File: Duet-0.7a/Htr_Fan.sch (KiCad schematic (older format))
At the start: 30 parts, among them J27 TP

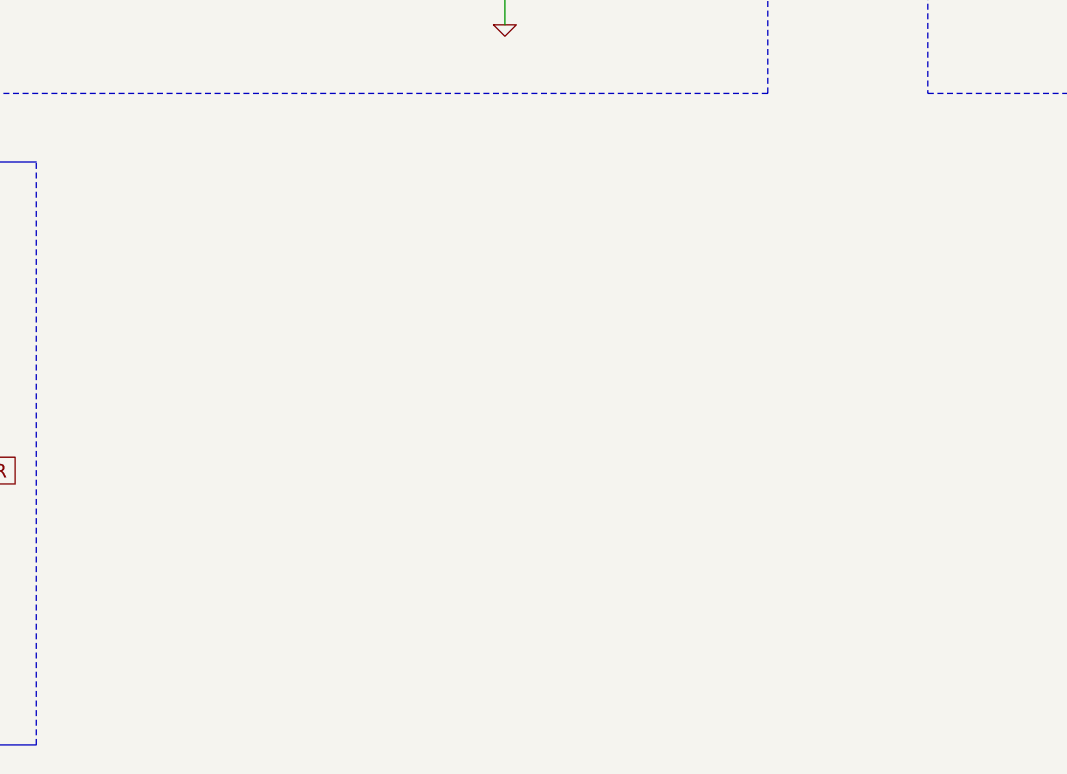
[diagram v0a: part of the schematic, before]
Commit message: Tell-tale LEDs added to Duet 0.7a.
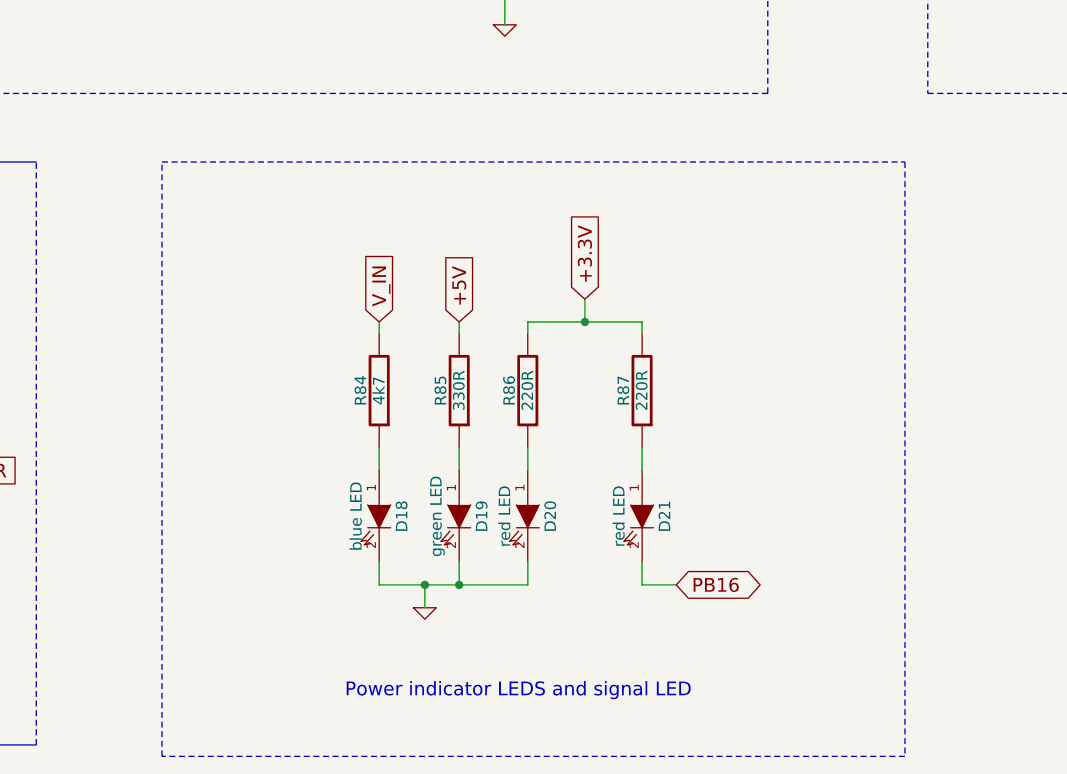
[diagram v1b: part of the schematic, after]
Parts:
- added D18: blue LED, symbol LED
- added D19: green LED, symbol LED
- added D20, D21: red LED, symbol LED
- added R84: 4k7, symbol R
- added R85: 330R, symbol R
- added R86, R87: 220R, symbol R
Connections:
- net labels added: PB16
- wire segments 87 -> 104
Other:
- note added: "Power indicator LEDS and signal LED"
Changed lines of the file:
@@
 LIBS:FE
 LIBS:Duet0.7-cache
-EELAYER 27 0
+EELAYER 24 0
 EELAYER END
 $Descr A3 16535 11693
@@
 FAN0-
 $Comp
-L GND #PWR56
+L GND #PWR054
 U 1 1 5090541F
 P 11600 4450
-F 0 "#PWR56" H 11600 4450 30  0001 C CNN
+F 0 "#PWR054" H 11600 4450 30  0001 C CNN
 F 1 "GND" H 11600 4380 30  0001 C CNN
 F 2 "" H 11600 4450 60  0001 C CNN
@@
 $EndComp
 $Comp
-L GND #PWR55
+L GND #PWR055
 U 1 1 50905416
 P 7400 4450
-F 0 "#PWR55" H 7400 4450 30  0001 C CNN
+F 0 "#PWR055" H 7400 4450 30  0001 C CNN
 F 1 "GND" H 7400 4380 30  0001 C CNN
 F 2 "" H 7400 4450 60  0001 C CNN
@@
 BED-
 $Comp
-L GND #PWR54
+L GND #PWR056
 U 1 1 5064BB75
 P 3300 4450
-F 0 "#PWR54" H 3300 4450 30  0001 C CNN
+F 0 "#PWR056" H 3300 4450 30  0001 C CNN
 F 1 "GND" H 3300 4380 30  0001 C CNN
 F 2 "" H 3300 4450 60  0001 C CNN
@@
 Text GLabel 2250 1800 1    60   Input ~ 0
 +5V
+Wire Wire Line
+	6850 6300 6850 6400
+Wire Wire Line
+	6850 5800 6850 5750
+Wire Wire Line
+	6850 6800 6850 6900
+$Comp
+L LED D18
+U 1 1 5491B59F
+P 6850 6600
+F 0 "D18" H 6850 6700 50  0000 C CNN
+F 1 "blue LED" H 6850 6500 50  0000 C CNN
+F 2 "" H 6850 6600 60  0001 C CNN
+F 3 "" H 6850 6600 60  0001 C CNN
+	1    6850 6600
+	0    1    1    0
+$EndComp
+$Comp
+L R R84
+U 1 1 5491B5A5
+P 6850 6050
+F 0 "R84" V 6930 6050 50  0000 C CNN
+F 1 "4k7" V 6850 6050 50  0000 C CNN
+F 2 "" H 6850 6050 60  0001 C CNN
+F 3 "" H 6850 6050 60  0001 C CNN
+	1    6850 6050
+	-1   0    0    1
+$EndComp
+Wire Wire Line
+	7200 6300 7200 6400
+Wire Wire Line
+	7200 5800 7200 5750
+Wire Wire Line
+	7200 6800 7200 6900
+$Comp
+L LED D19
+U 1 1 5491B5BB
+P 7200 6600
+F 0 "D19" H 7200 6700 50  0000 C CNN
+F 1 "green LED" H 7200 6500 50  0000 C CNN
+F 2 "" H 7200 6600 60  0001 C CNN
+F 3 "" H 7200 6600 60  0001 C CNN
+	1    7200 6600
+	0    1    1    0
+$EndComp
+$Comp
+L R R85
+U 1 1 5491B5C1
+P 7200 6050
+F 0 "R85" V 7280 6050 50  0000 C CNN
+F 1 "330R" V 7200 6050 50  0000 C CNN
+F 2 "" H 7200 6050 60  0001 C CNN
+F 3 "" H 7200 6050 60  0001 C CNN
+	1    7200 6050
+	-1   0    0    1
+$EndComp
+Wire Wire Line
+	7500 6300 7500 6400
+Wire Wire Line
+	7500 5800 7500 5750
+Wire Wire Line
+	7500 6900 7500 6800
+$Comp
+L LED D20
+U 1 1 5491B5CA
+P 7500 6600
+F 0 "D20" H 7500 6700 50  0000 C CNN
+F 1 "red LED" H 7500 6500 50  0000 C CNN
+F 2 "" H 7500 6600 60  0001 C CNN
+F 3 "" H 7500 6600 60  0001 C CNN
+	1    7500 6600
+	0    1    1    0
+$EndComp
+$Comp
+L R R86
+U 1 1 5491B5D0
+P 7500 6050
+F 0 "R86" V 7580 6050 50  0000 C CNN
+F 1 "220R" V 7500 6050 50  0000 C CNN
+F 2 "" H 7500 6050 60  0001 C CNN
+F 3 "" H 7500 6050 60  0001 C CNN
+	1    7500 6050
+	-1   0    0    1
+$EndComp
+Wire Wire Line
+	8000 6300 8000 6400
+Wire Wire Line
+	8000 5800 8000 5750
+Wire Wire Line
+	8000 6800 8000 6900
+$Comp
+L LED D21
+U 1 1 5491B5D9
+P 8000 6600
+F 0 "D21" H 8000 6700 50  0000 C CNN
+F 1 "red LED" H 8000 6500 50  0000 C CNN
+F 2 "" H 8000 6600 60  0001 C CNN
+F 3 "" H 8000 6600 60  0001 C CNN
+	1    8000 6600
+	0    1    1    0
+$EndComp
+$Comp
+L R R87
+U 1 1 5491B5DF
+P 8000 6050
+F 0 "R87" V 8080 6050 50  0000 C CNN
+F 1 "220R" V 8000 6050 50  0000 C CNN
+F 2 "" H 8000 6050 60  0001 C CNN
+F 3 "" H 8000 6050 60  0001 C CNN
+	1    8000 6050
+	-1   0    0    1
+$EndComp
+Wire Wire Line
+	6850 6900 7500 6900
+Connection ~ 7200 6900
+Wire Wire Line
+	7050 6900 7050 7000
+Connection ~ 7050 6900
+Wire Wire Line
+	8000 5750 7500 5750
+Wire Wire Line
+	7750 5750 7750 5650
+Connection ~ 7750 5750
+Text GLabel 6850 5750 1    60   Input ~ 0
+V_IN
+Text GLabel 7200 5750 1    60   Input ~ 0
++5V
+Text GLabel 7750 5650 1    60   Input ~ 0
++3.3V
+$Comp
+L GND #PWR057
+U 1 1 5491B8B7
+P 7050 7000
+F 0 "#PWR057" H 7050 7000 30  0001 C CNN
+F 1 "GND" H 7050 6930 30  0001 C CNN
+F 2 "" H 7050 7000 60  0001 C CNN
+F 3 "" H 7050 7000 60  0001 C CNN
+	1    7050 7000
+	1    0    0    -1
+$EndComp
+Text GLabel 8150 6900 2    60   BiDi ~ 0
+PB16
+Wire Wire Line
+	8000 6900 8150 6900
+Wire Notes Line
+	5900 5050 9150 5050
+Wire Notes Line
+	9150 5050 9150 7650
+Wire Notes Line
+	9150 7650 5900 7650
+Wire Notes Line
+	5900 7650 5900 5050
+Text Notes 6700 7400 0    60   ~ 0
+Power indicator LEDS and signal LED
 $EndSCHEMATC

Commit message: Updating Duet 0.7a...
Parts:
- R85: value 330R -> 680R
- R86, R87: value 220R -> 470R
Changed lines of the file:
@@
 LIBS:FE
 LIBS:Duet0.7-cache
-EELAYER 24 0
+EELAYER 27 0
 EELAYER END
 $Descr A3 16535 11693
@@
 Sheet 6 7
 Title "Duet"
-Date "15 dec 2014"
+Date "17 dec 2014"
 Rev "0.7"
 Comp "Think3DPrint3D, RepRapPro"
@@
 P 7200 6050
 F 0 "R85" V 7280 6050 50  0000 C CNN
-F 1 "330R" V 7200 6050 50  0000 C CNN
+F 1 "680R" V 7200 6050 50  0000 C CNN
 F 2 "" H 7200 6050 60  0001 C CNN
 F 3 "" H 7200 6050 60  0001 C CNN
@@
 P 7500 6050
 F 0 "R86" V 7580 6050 50  0000 C CNN
-F 1 "220R" V 7500 6050 50  0000 C CNN
+F 1 "470R" V 7500 6050 50  0000 C CNN
 F 2 "" H 7500 6050 60  0001 C CNN
 F 3 "" H 7500 6050 60  0001 C CNN
@@
 P 8000 6050
 F 0 "R87" V 8080 6050 50  0000 C CNN
-F 1 "220R" V 8000 6050 50  0000 C CNN
+F 1 "470R" V 8000 6050 50  0000 C CNN
 F 2 "" H 8000 6050 60  0001 C CNN
 F 3 "" H 8000 6050 60  0001 C CNN
